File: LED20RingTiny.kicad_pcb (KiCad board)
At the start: 2 copper layers, 21 parts, among them IC1 ATTINY45-P

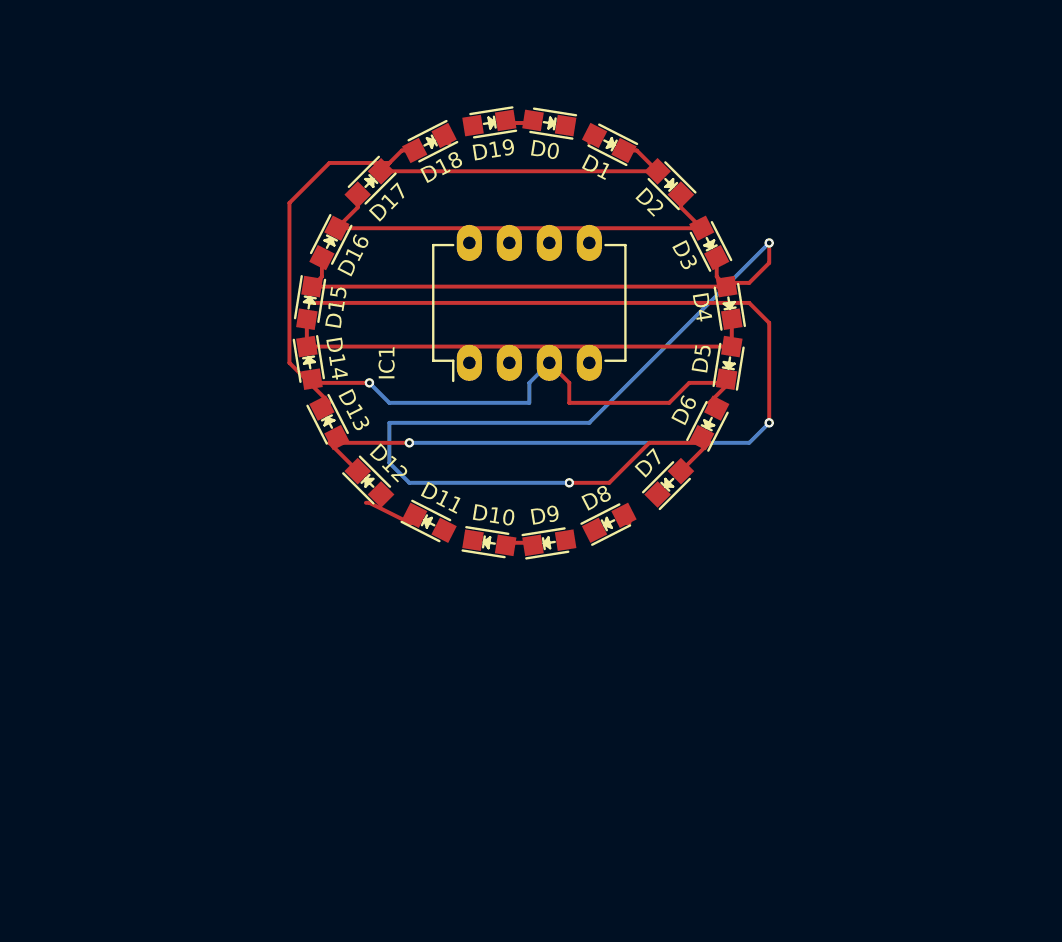
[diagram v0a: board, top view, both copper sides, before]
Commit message: Align LEDs on 5mils grid
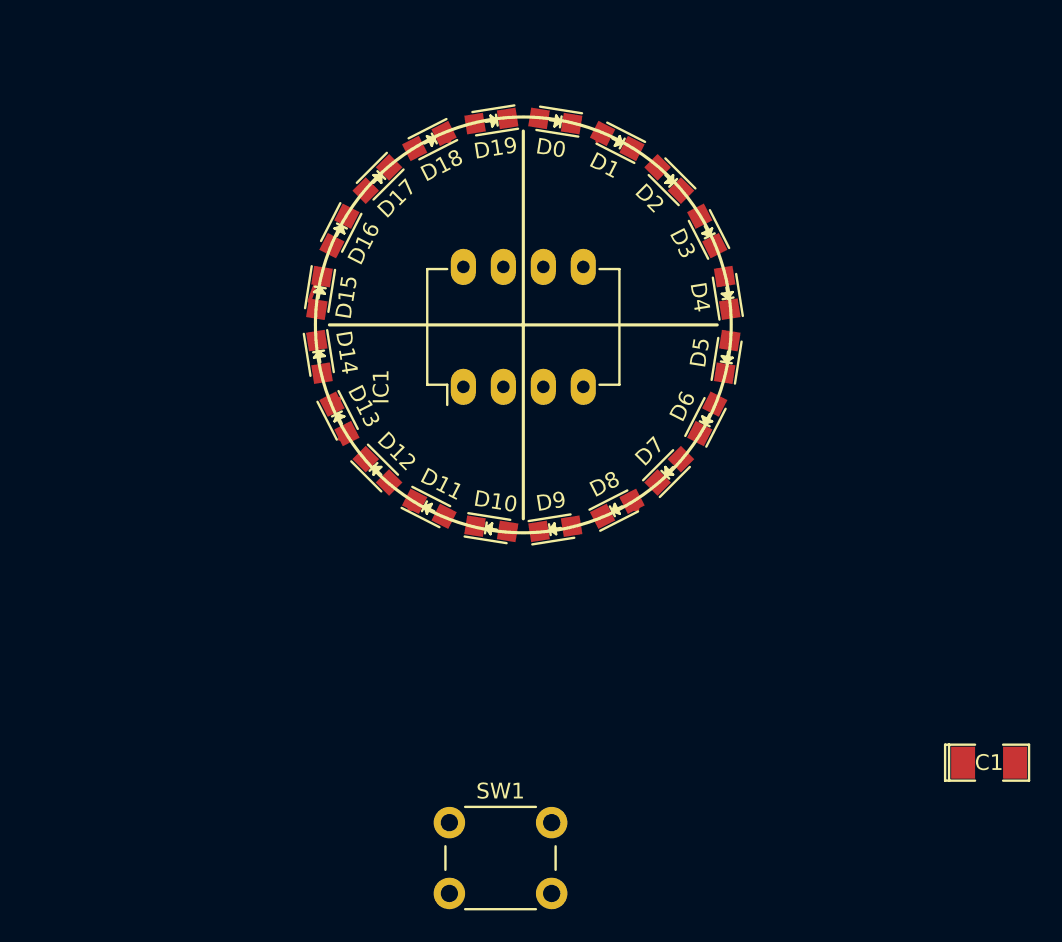
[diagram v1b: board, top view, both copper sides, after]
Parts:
- added C1: 10µ, SMD_Packages:SMD-1206_Pol, F.Cu at (209.6, 133.3)
- added SW1: SW_Push, Buttons_Switches_THT:SW_PUSH_6mm, F.Cu at (175.3, 137.2)
- moved IC1 1.57 mm to (176.1, 109.5)
- moved D8 1.02 mm to (185.9, 117.2)
- moved D16 0.99 mm to (168.3, 99.6)
- moved D9 0.97 mm to (182.0, 118.5)
- moved D12 0.92 mm to (170.7, 114.8)
- moved D15 0.90 mm to (167.0, 103.5)
- moved D10 0.90 mm to (177.9, 118.5)
- moved D11 0.89 mm to (174.0, 117.2)
- moved D3 0.77 mm to (191.6, 99.6)
- moved D7 0.76 mm to (189.2, 114.8)
- moved D14 0.74 mm to (167.0, 107.6)
- moved D13 0.68 mm to (168.3, 111.5)
- moved D4 0.65 mm to (192.9, 103.5)
- moved D17 0.57 mm to (170.7, 96.3)
- moved D1 0.52 mm to (185.9, 93.9)
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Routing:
- net Net-(D12-Pad1): track 162.0 -> 1.67 mm, vias 4 -> 0
- net Net-(D1-Pad1): track 80.5 -> 2.68 mm, vias 1 -> 0
- net Net-(D0-Pad2): track 35.4 -> 3.12 mm
- net Net-(D10-Pad1): track 28.5 -> 0.00 mm
- net Net-(D0-Pad1): track 6.40 -> 2.83 mm

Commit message: Add some Traces
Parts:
- IC1: footprint Housings_DIP:DIP-8_W7.62mm_LongPads -> Housings_SOIC:SOIJ-8_5.3x5.3mm_Pitch1.27mm
- moved C1 51.9 mm to (158.6, 123.3)
- moved IC1 5.48 mm to (180.0, 105.5)
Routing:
- net Net-(D10-Pad1): track 0.00 -> 64.9 mm, vias 0 -> 2
- net Net-(D1-Pad1): track 2.68 -> 56.9 mm
- net Net-(D0-Pad1): track 2.83 -> 38.0 mm
- net Net-(D0-Pad2): track 3.12 -> 37.3 mm
- net Net-(D12-Pad1): track 1.67 -> 28.1 mm

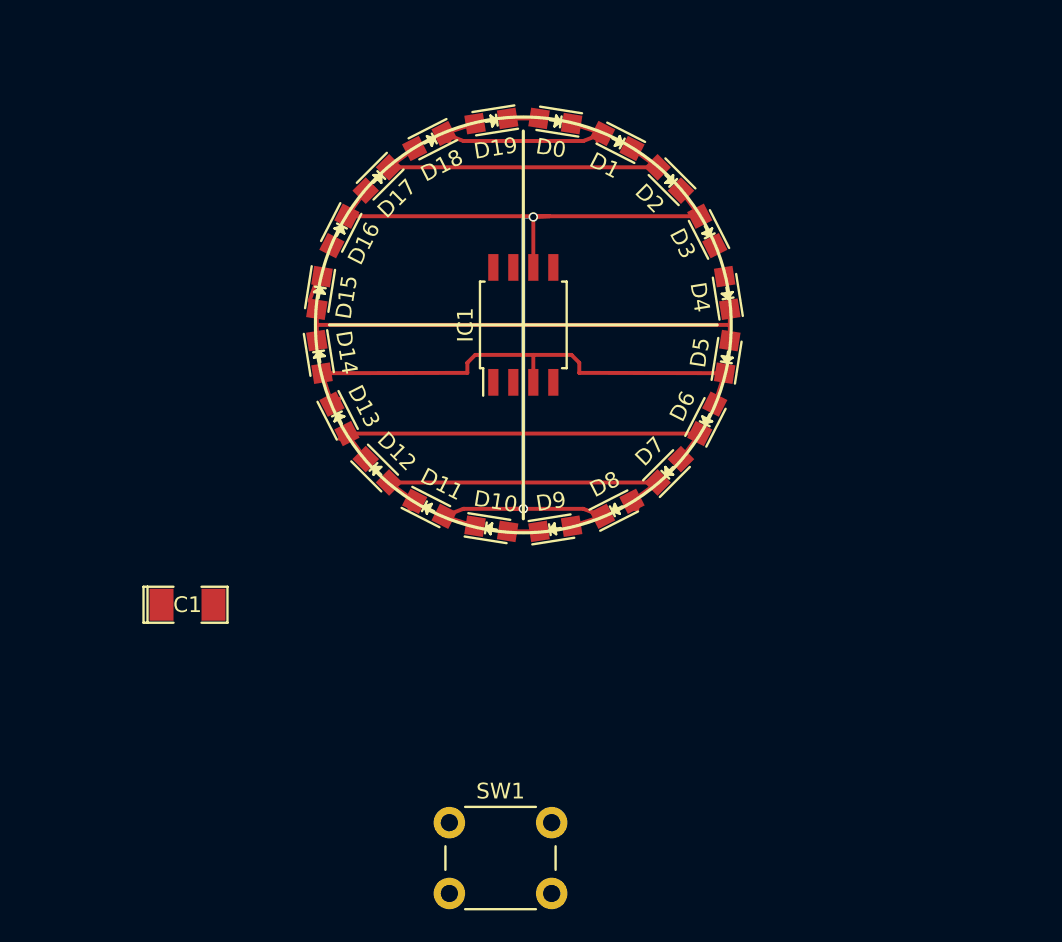
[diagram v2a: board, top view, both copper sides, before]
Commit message: Exact LED locations on circle.
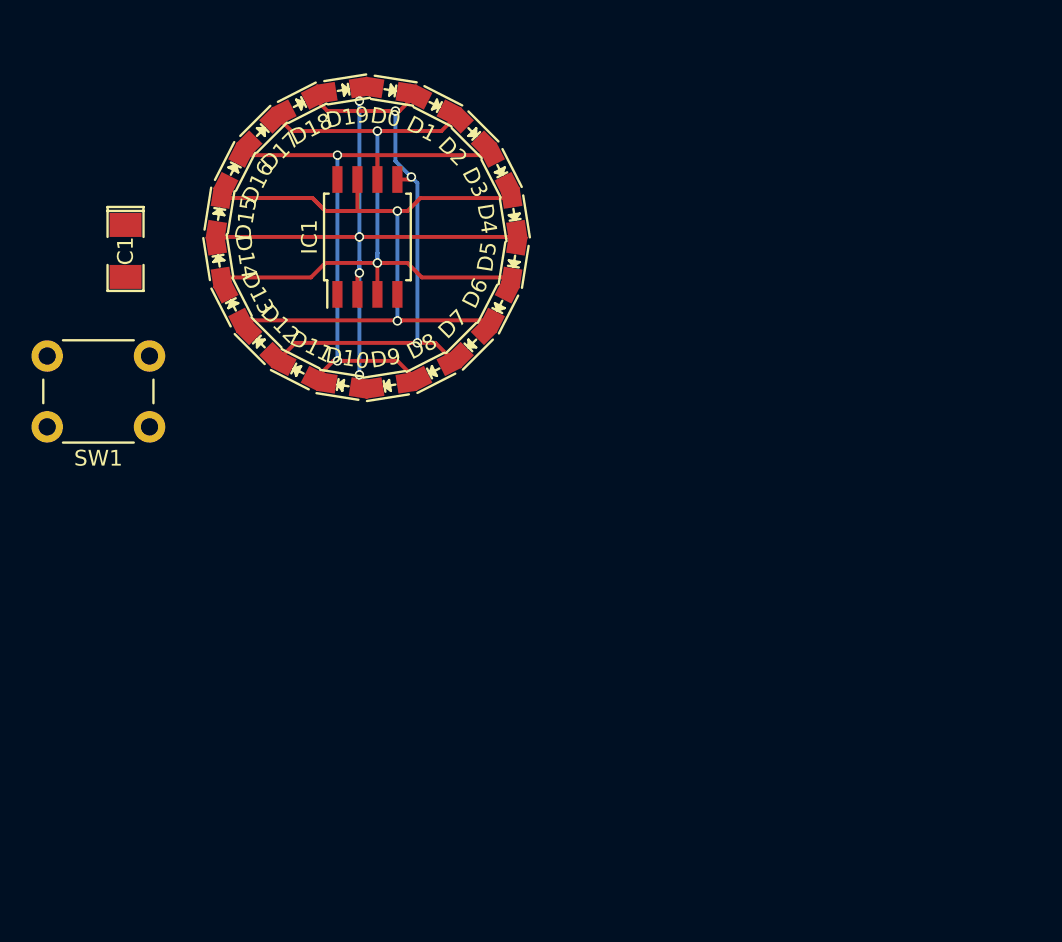
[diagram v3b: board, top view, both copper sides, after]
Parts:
- moved SW1 31.5 mm to (156.2, 112.0), turned to 180 degrees
- moved C1 22.8 mm to (154.7, 100.8), turned to 270 degrees
- moved D6 15.0 mm to (178.5, 104.3)
- moved D7 14.9 mm to (176.7, 106.7)
- moved D5 14.8 mm to (179.4, 101.5)
- moved D8 14.5 mm to (174.3, 108.5)
- moved D4 14.4 mm to (179.4, 98.5)
- moved D9 13.9 mm to (171.5, 109.4)
- moved D3 13.7 mm to (178.5, 95.7)
- moved D10 13.1 mm to (168.5, 109.4)
- moved D2 12.9 mm to (176.7, 93.3)
- moved D11 12.1 mm to (165.7, 108.5)
- moved D1 11.8 mm to (174.3, 91.5)
- moved IC1 11.4 mm to (170.1, 99.9)
- moved D12 11.0 mm to (163.3, 106.7)
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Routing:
- net Net-(D12-Pad1): track 28.1 -> 60.7 mm, vias 0 -> 2
- net Net-(D10-Pad1): track 64.9 -> 40.6 mm
- net Net-(D1-Pad1): track 56.9 -> 46.4 mm, vias 0 -> 2
- net Net-(D0-Pad2): track 37.3 -> 43.5 mm, vias 0 -> 4
- net Net-(D0-Pad1): track 38.0 -> 37.3 mm, vias 0 -> 3

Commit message: Improve
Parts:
- added BT1: Battery_Cell, Connectors:CR2032V, B.Cu at (170.1, 113.0)
- C1: moved to B.Cu
- SW1: footprint Buttons_Switches_THT:SW_PUSH_6mm -> Buttons_Switches_SMD:SW_SPST_KMR2
- moved C1 27.4 mm to (179.3, 112.9)
- moved SW1 4.97 mm to (161.2, 112.4), turned to 90 degrees
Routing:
- net GND: track 0.00 -> 37.0 mm, vias 0 -> 2
- net +3V3: track 0.00 -> 30.6 mm, vias 0 -> 2
- net Net-(IC1-Pad1): track 0.00 -> 18.4 mm, vias 0 -> 2
- net Net-(D10-Pad1): track 40.6 -> 42.5 mm
- net Net-(D0-Pad1): track 37.3 -> 38.9 mm
- net Net-(D0-Pad2): track 43.5 -> 44.1 mm
- added copper zone on B.Cu, net +3V3
- added copper zone on B.Cu, net GND
- added copper zone on F.Cu, net GND
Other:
- board text added: "jens@4k2.de"
- board text added: "©2017"
